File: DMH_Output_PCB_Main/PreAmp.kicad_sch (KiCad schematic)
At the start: 39 parts, among them J13 Conn_01x06, J28 Conn_01x06, U16 NE5532, U17 NE5532, U18 NE5532, U19 NE5532

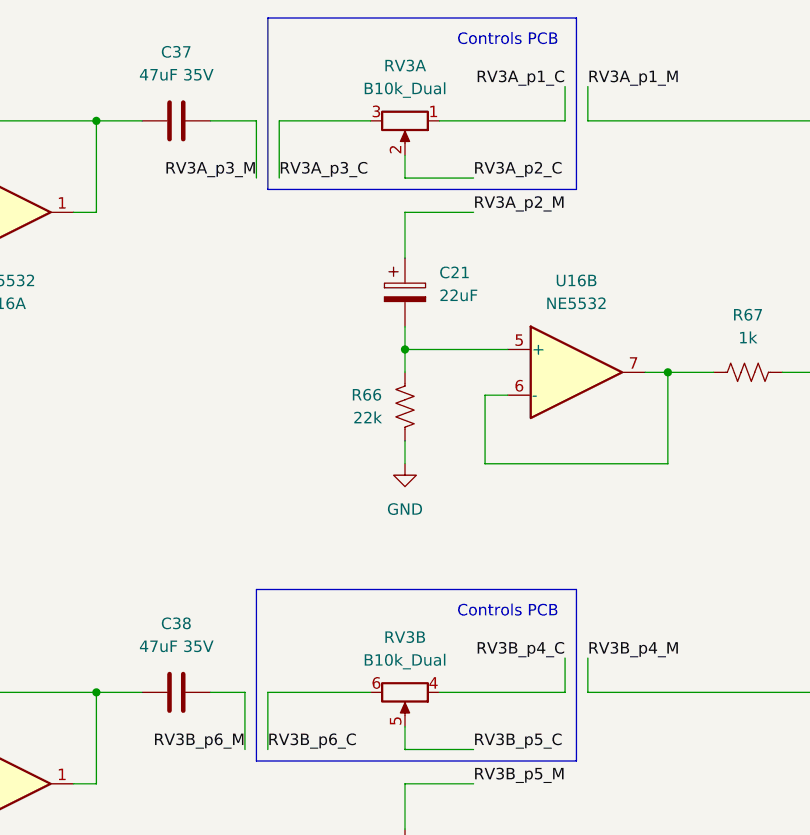
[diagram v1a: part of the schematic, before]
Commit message: Replaced jack symbols with 5pin ones
Also updated Meter LED current source resistor to 75R
Also increased LED guiding PCB mounting holes to M2.5
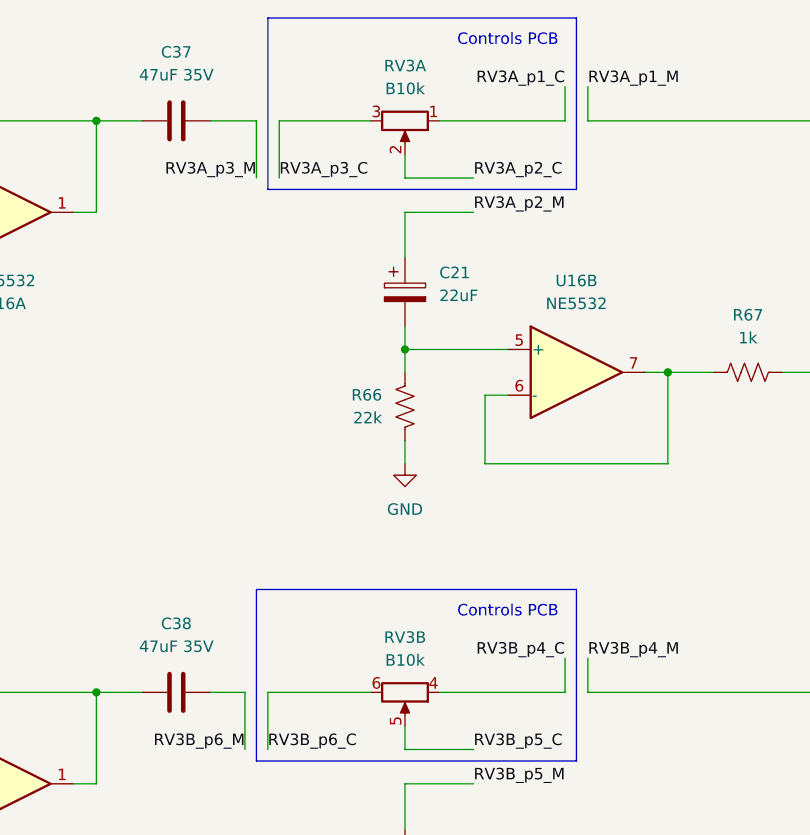
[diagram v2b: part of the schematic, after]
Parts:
- RV3: value B10k_Dual -> B10k; footprint Potentiometer_THT:Potentiometer_Alpha_RD902F-40-00D_Dual_Vertical -> SynthStuff:Potentiometer_Alpha_RD902F-40-00D_Dual_Vertical
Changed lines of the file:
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@@
 			)
 		)
-		(property "Value" "B10k_Dual"
+		(property "Value" "B10k"
 			(at 127 21.844 90)
 			(show_name no)
@@
 			)
 		)
-		(property "Footprint" "Potentiometer_THT:Potentiometer_Alpha_RD902F-40-00D_Dual_Vertical"
+		(property "Footprint" "SynthStuff:Potentiometer_Alpha_RD902F-40-00D_Dual_Vertical"
 			(at 127 25.4 0)
 			(hide yes)
@@
 					(bold yes)
 					(italic yes)
+				)
+			)
+		)
+		(property "Sim.Library" "${KICAD9_SYMBOL_DIR}/Simulation_SPICE.sp"
+			(at 127 25.4 0)
+			(hide yes)
+			(show_name no)
+			(do_not_autoplace no)
+			(effects
+				(font
+					(size 1.27 1.27)
+				)
+			)
+		)
+		(property "Sim.Name" "pot_dual"
+			(at 127 25.4 0)
+			(hide yes)
+			(show_name no)
+			(do_not_autoplace no)
+			(effects
+				(font
+					(size 1.27 1.27)
+				)
+			)
+		)
+		(property "Sim.Device" "SUBCKT"
+			(at 127 25.4 0)
+			(hide yes)
+			(show_name no)
+			(do_not_autoplace no)
+			(effects
+				(font
+					(size 1.27 1.27)
+				)
+			)
+		)
+		(property "Sim.Pins" "1=r1A 2=wA 3=r0A 4=r1B 5=wB 6=r0B"
+			(at 127 25.4 0)
+			(hide yes)
+			(show_name no)
+			(do_not_autoplace no)
+			(effects
+				(font
+					(size 1.27 1.27)
+				)
+			)
+		)
+		(property "Sim.Params" "Rtot=1 wpos=0.4"
+			(at 127 25.4 0)
+			(hide yes)
+			(show_name no)
+			(do_not_autoplace no)
+			(effects
+				(font
+					(size 1.27 1.27)
 				)
 			)
@@
 			)
 		)
-		(property "Value" "B10k_Dual"
+		(property "Value" "B10k"
 			(at 127 85.344 90)
 			(show_name no)
@@
 			)
 		)
-		(property "Footprint" "Potentiometer_THT:Potentiometer_Alpha_RD902F-40-00D_Dual_Vertical"
+		(property "Footprint" "SynthStuff:Potentiometer_Alpha_RD902F-40-00D_Dual_Vertical"
 			(at 127 88.9 0)
 			(hide yes)
@@
 				)
 			)
+		)
+		(property "Sim.Library" "${KICAD9_SYMBOL_DIR}/Simulation_SPICE.sp"
+			(at 127 88.9 0)
+			(hide yes)
+			(show_name no)
+			(do_not_autoplace no)
+			(effects
+				(font
+					(size 1.27 1.27)
+				)
+			)
+		)
+		(property "Sim.Name" "pot_dual"
+			(at 127 88.9 0)
+			(hide yes)
+			(show_name no)
+			(do_not_autoplace no)
+			(effects
+				(font
+					(size 1.27 1.27)
+				)
+			)
+		)
+		(property "Sim.Device" "SUBCKT"
+			(at 127 88.9 0)
+			(hide yes)
+			(show_name no)
+			(do_not_autoplace no)
+			(effects
+				(font
+					(size 1.27 1.27)
+				)
+			)
+		)
+		(property "Sim.Pins" "1=r1A 2=wA 3=r0A 4=r1B 5=wB 6=r0B"
+			(at 127 88.9 0)
+			(hide yes)
+			(show_name no)
+			(do_not_autoplace no)
+			(effects
+				(font
+					(size 1.27 1.27)
+				)
+			)
+		)
+		(property "Sim.Params" "Rtot=1 wpos=0.4"
+			(at 127 88.9 0)
+			(hide yes)
+			(show_name no)
+			(do_not_autoplace no)
+			(effects
+				(font
+					(size 1.27 1.27)
+				)
+			)

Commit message: Prepped for Main PCB design
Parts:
- added J33: Conn_01x06, Connector_PinHeader_2.54mm:PinHeader_1x06_P2.54mm_Vertical, symbol Connector_Generic:Conn_01x06
- added J35: Conn_01x04_PinHeader, Connector_PinSocket_2.54mm:PinSocket_1x04_P2.54mm_Vertical, symbol SynthStuff:Conn_01x04_PinHeader
- added J36: Conn_01x04_PinHeader, Connector_PinHeader_2.54mm:PinHeader_1x04_P2.54mm_Vertical, symbol SynthStuff:Conn_01x04_PinHeader
- J28: footprint Connector_PinHeader_2.54mm:PinHeader_1x06_P2.54mm_Vertical -> Connector_PinSocket_2.54mm:PinSocket_1x06_P2.54mm_Vertical
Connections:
- net RV3A_p1_M: no longer C19.2, R68.2, R76.1, U17.1
- net RV3A_p2_M: no longer C21.1
- net RV3A_p3_M: no longer C37.2
- net RV3B_p4_M: no longer C35.2, R73.2, R79.1, U19.1
- net RV3B_p5_M: no longer C20.1
- net RV3B_p6_M: no longer C38.2
- net L_Euro_OUT: no longer names the net of R70.2
- net L_Euro_OUT: now also J36.3 (Pin_3)
- net L_Ext_IN: no longer names the net of R63.1
- net L_Ext_IN: now also J36.1 (Pin_1)
- net R_Euro_OUT: no longer names the net of R74.2
- net R_Euro_OUT: now also J36.4 (Pin_4)
- net R_Ext_IN: no longer names the net of R60.1
- net R_Ext_IN: now also J36.2 (Pin_2)
- new net L_Euro_OUT_M: J35.3 (Pin_3)
- new net L_Ext_IN_M: J35.1 (Pin_1)
- new net RV3A_p1_MZ: C19.2, J33.1 (Pin_1), R68.2, R76.1, U17.1
- new net RV3A_p2_MZ: C21.1, J33.2 (Pin_2)
- new net RV3A_p3_MZ: C37.2, J33.3 (Pin_3)
- new net RV3B_p4_MZ: C35.2, J33.6 (Pin_6), R73.2, R79.1, U19.1
- new net RV3B_p5_MZ: C20.1, J33.5 (Pin_5)
- new net RV3B_p6_MZ: C38.2, J33.4 (Pin_4)
- new net R_Euro_OUT_M: J35.4 (Pin_4)
- new net R_Ext_IN_M: J35.2 (Pin_2)
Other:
- note added: "Mezanine PCB"
- moved on the sheet: J13, J28
